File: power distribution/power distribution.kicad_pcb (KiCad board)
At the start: 2 copper layers, 77.9 x 100 mm, 216 parts, among them J1 HEATER6, J10 TH0, J11 TH4, J13 HEATER4, J14 TH1, J15 TH5, J17 Conn_01x02_Socket, J18 Conn_01x02_Socket, J19 HEATER5, J2 HEATER0, J20 TH2, J21 TH6, J22 TH3, J23 TH7, J3 HEATER7, J4 SWD, J5 HEATER1, J6 HEATER2, J7 UART, J8 USB_C_Receptacle_USB2.0_14P, J9 HEATER3, M2 MountingHole_2.2mm_M2_DIN965_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, Q1 AOD4184A, Q2 AOD4184A, Q3 AOD4184A, Q4 AOD4184A, Q5 AOD4184A, Q6 AOD4184A, Q7 AOD4184A, Q8 AOD4184A, SW1 SW_Push, SW2 SW_Push, U1 TPS54202DDC, U10 UCC27511ADBV, U11 TLV73333PDBV, U12 TLV73333PDBV, U13 UCC27511ADBV, U14 UCC27511ADBV, U15 UCC27511ADBV, U2 UCC27511ADBV, U3 UCC27511ADBV, U4 STM32F030K6Tx, U5 TPS54202DDC, U6 UCC27511ADBV, U7 UCC27511ADBV, U8 SRV05-4, U9 CH340E, Y1 24MHz

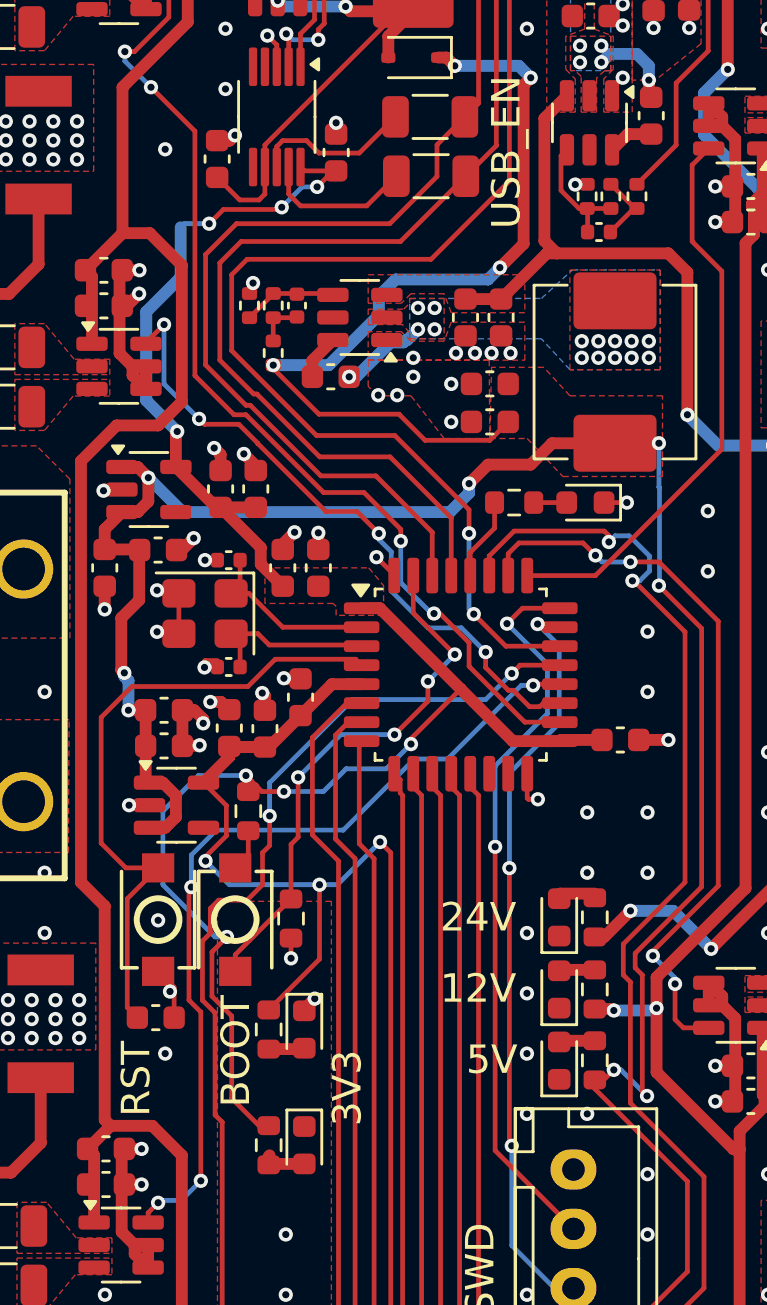
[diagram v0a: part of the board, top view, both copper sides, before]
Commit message: fix: fixed uart connections, usb flashing requires flashing via UART on PA9/PA10
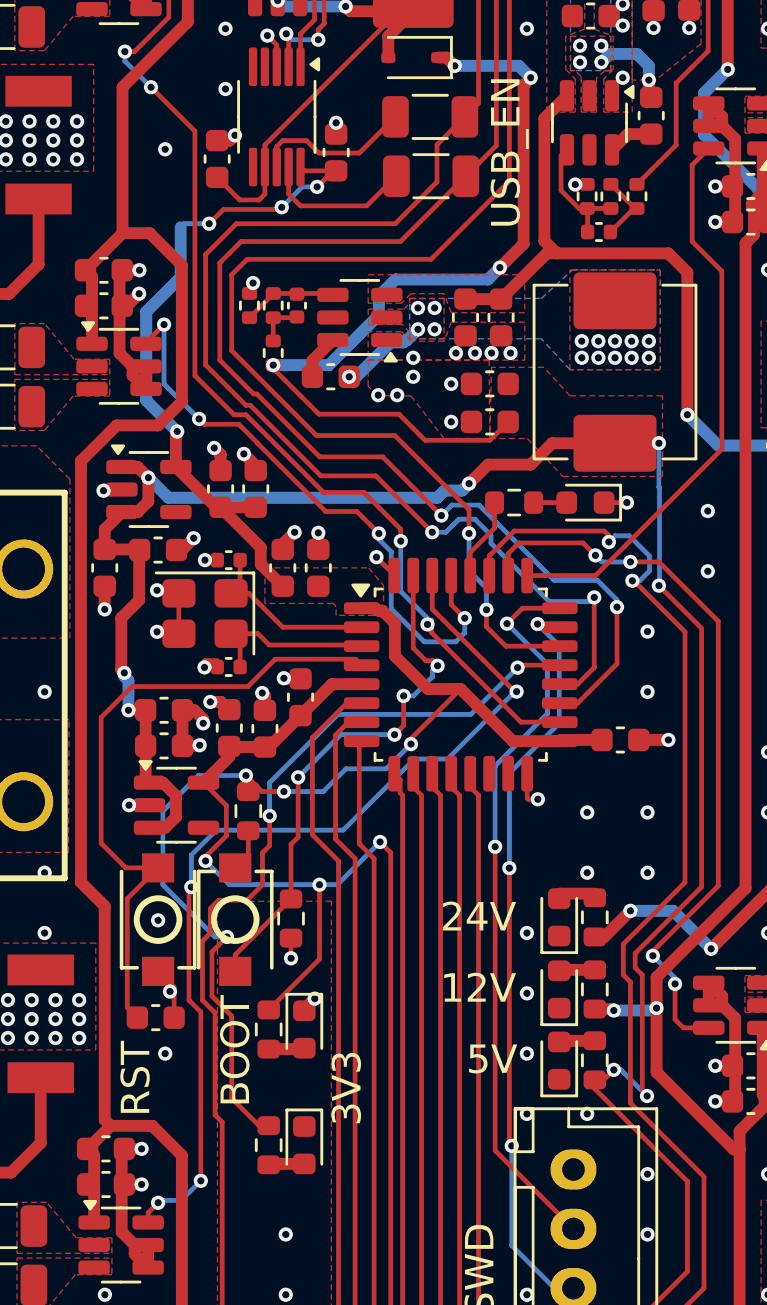
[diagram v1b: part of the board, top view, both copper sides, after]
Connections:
- U4 pad 19: HEATER1 -> TX
- U4 pad 20: HEATER2 -> RX
- U4 pad 29: TX -> HEATER1
- U4 pad 30: RX -> HEATER2
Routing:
- net TX: track 51.1 -> 63.4 mm, vias 0 -> 2
- net RX: track 49.8 -> 61.5 mm, vias 0 -> 2
- net HEATER2: track 35.7 -> 40.2 mm
- net HEATER1: track 27.5 -> 24.8 mm
- net +3.3V: track 73.3 -> 74.1 mm
- net +5V: track 130.1 -> 129.3 mm

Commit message: chore: update github journal with obsidian journal
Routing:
- net GND: vias 422 -> 423
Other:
- board text added: "CLK"
- board text added: "IO"

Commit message: chore: add images
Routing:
- net HEATER1: track 24.8 -> 23.6 mm
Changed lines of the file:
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@@
-	)
-	(segment
-		(start 138.21401 65.28599)
-		(end 138.975 64.525)
-		(width 0.2)
-		(layer "F.Cu")
-		(net 116)
 	)
 	(segment
@@
 	)
 	(segment
-		(start 140.677471 68.726)
-		(end 140.450735 68.499265)
+		(start 138.22901 65.35)
+		(end 138.21401 65.335)
 		(width 0.2)
 		(layer "F.Cu")
@@
 	)
 	(segment
-		(start 138.21401 65.335)
-		(end 138.21401 65.28599)
+		(start 140.677471 68.726)
+		(end 140.450735 68.499265)
 		(width 0.2)
 		(layer "F.Cu")
@@
 		(start 142.925 69.525)
 		(end 142.126 68.726)
+		(width 0.2)
+		(layer "F.Cu")
+		(net 116)
+	)
+	(segment
+		(start 138.975 65.35)
+		(end 138.22901 65.35)
 		(width 0.2)
 		(layer "F.Cu")
@@
 	)
 	(via
-		(at 138.975 64.525)
+		(at 138.975 65.35)
 		(size 0.6)
 		(drill 0.3)
 		(layers "F.Cu" "B.Cu")
-		(net 116)
-	)
-	(segment
-		(start 138.975 67.02353)
-		(end 138.975 64.525)
-		(width 0.2)
-		(layer "B.Cu")
 		(net 116)
 	)
@@
 		(start 148.025 73.574943)
 		(end 148.025 73.325)
+		(width 0.2)
+		(layer "B.Cu")
+		(net 116)
+	)
+	(segment
+		(start 138.975 67.02353)
+		(end 140.450735 68.499265)
 		(width 0.2)
 		(layer "B.Cu")
@@
 	)
 	(segment
-		(start 140.450735 68.499265)
+		(start 138.975 65.35)
 		(end 138.975 67.02353)
 		(width 0.2)
